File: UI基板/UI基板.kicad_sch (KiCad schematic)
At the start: 2 parts, among them U1 TFT_320x240

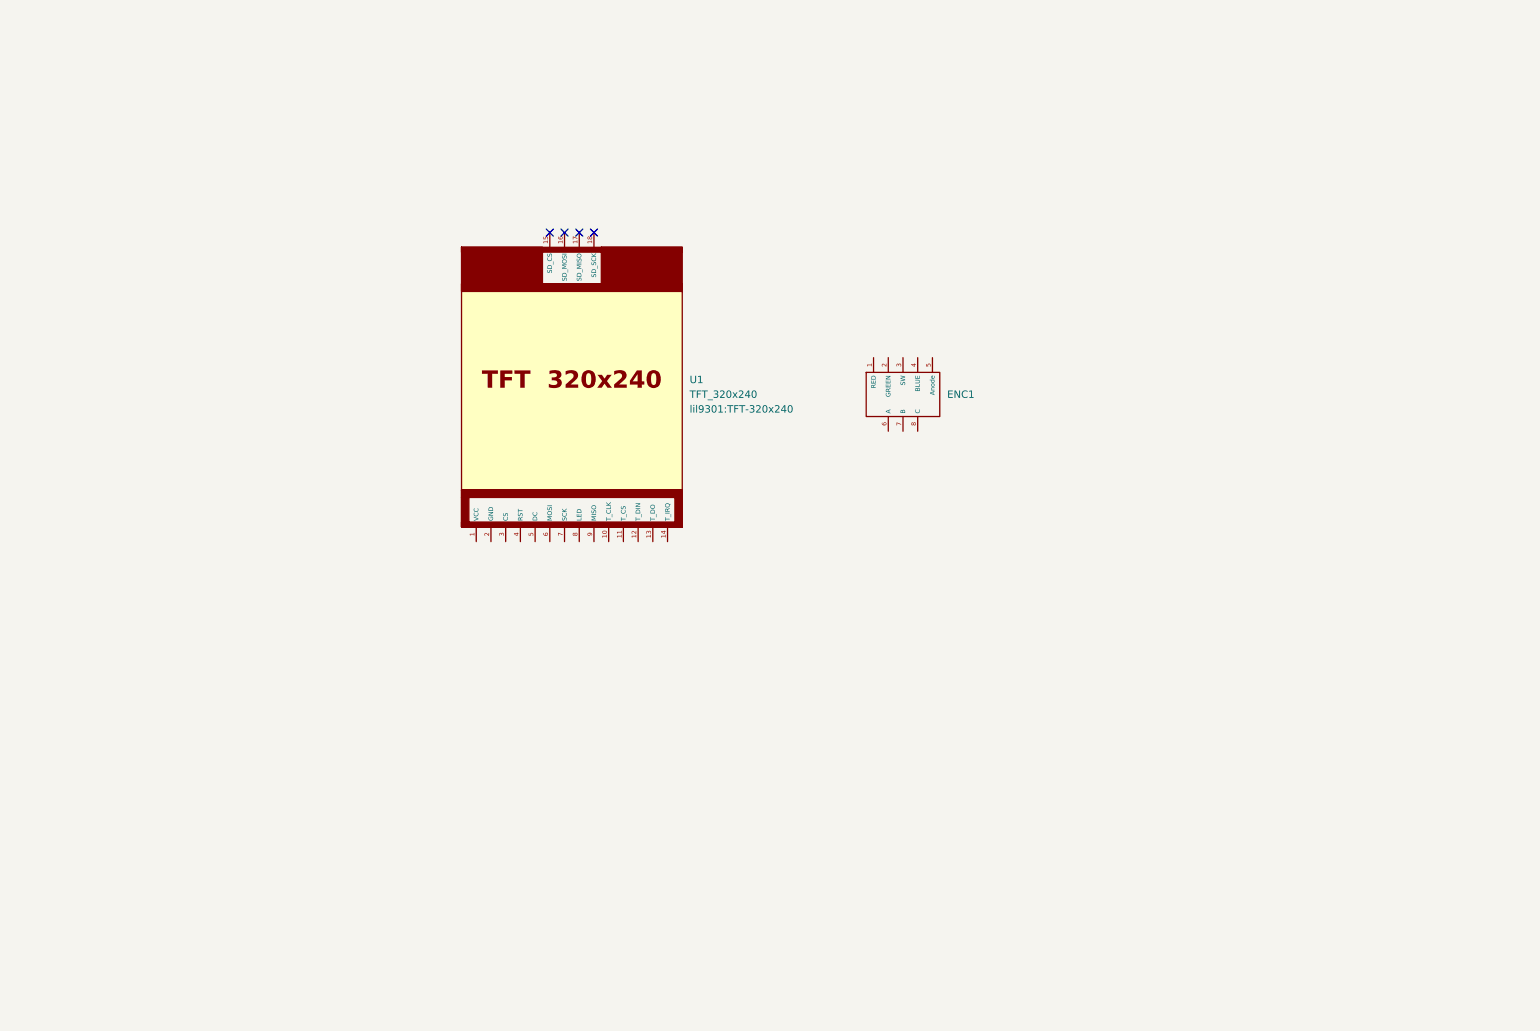
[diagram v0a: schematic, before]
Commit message: パスコンと保護ダイオードの追加
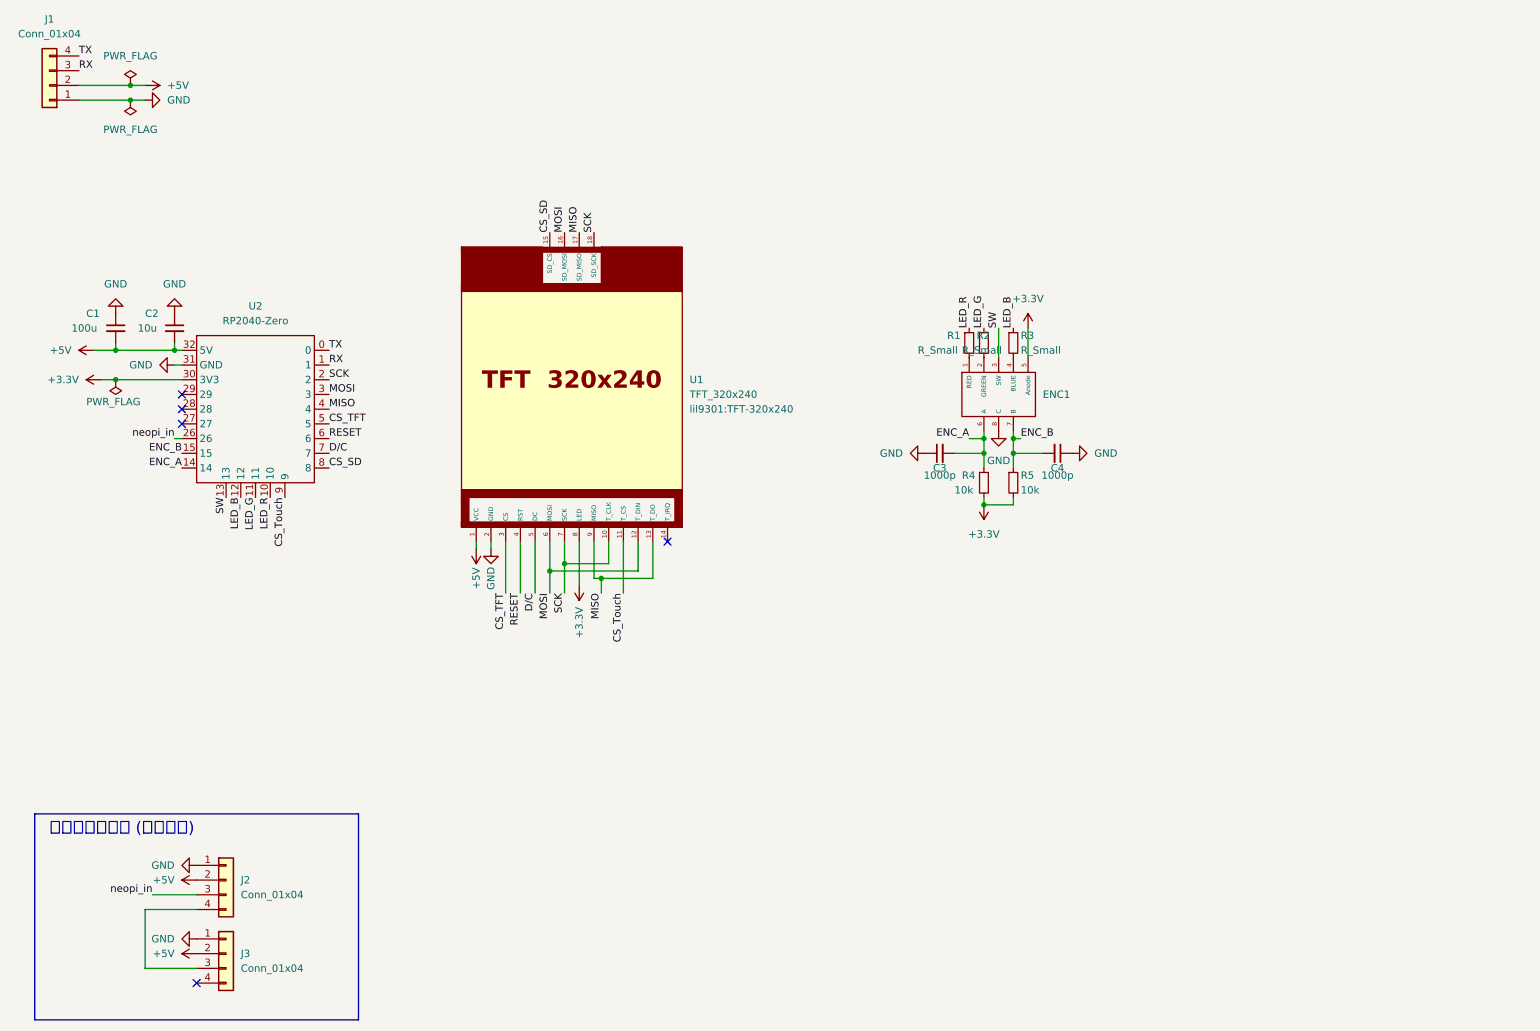
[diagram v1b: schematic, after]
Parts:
- added C1: 100u, Capacitor_THT:CP_Radial_D5.0mm_P2.50mm, symbol Device:C_Small
- added C2: 10u, Resistor_SMD:R_0603_1608Metric_Pad0.98x0.95mm_HandSolder, symbol Device:C_Small
- added C3, C4: 1000p, Capacitor_SMD:C_0603_1608Metric_Pad1.08x0.95mm_HandSolder, symbol Device:C_Small
- added J1, J2, J3: Conn_01x04, Connector_JST:JST_XH_S4B-XH-A_1x04_P2.50mm_Horizontal, symbol Connector_Generic:Conn_01x04
- added R1, R2, R3: R_Small, Resistor_SMD:R_0603_1608Metric_Pad0.98x0.95mm_HandSolder, symbol Device:R_Small
- added R4, R5: 10k, Resistor_SMD:R_0603_1608Metric_Pad0.98x0.95mm_HandSolder, symbol Device:R_Small
- added U2: RP2040-Zero, isw-kbd:RP2040-Zero-THT, symbol isw-mcu:RP2040-Zero
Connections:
- net +5V: now reaches U1.1 (VCC)
- net +5V: now also C1.2, C2.2, J1.2 (Pin_2), J2.2 (Pin_2), J3.2 (Pin_2), U2.32 (5V)
- net SCK: now reaches U1.10 (T_CLK)
- net SCK: now also U1.18 (SD_SCK), U1.7 (SCK), U2.2
- net CS_Touch: now reaches U1.11 (T_CS)
- net CS_Touch: now also U2.9
- net MOSI: now reaches U1.12 (T_DIN)
- net MOSI: now also U1.16 (SD_MOSI), U1.6 (MOSI), U2.3
- net MISO: now reaches U1.13 (T_DO)
- net MISO: now also U1.17 (SD_MISO), U1.9 (MISO), U2.4
- net CS_SD: now reaches U1.15 (SD_CS)
- net CS_SD: now also U2.8
- net GND: now reaches U1.2 (GND)
- net GND: now also ENC1.8 (C), C1.1, C2.1, C3.1, C4.1, J1.1 (Pin_1), J2.1 (Pin_1), J3.1 (Pin_1), U2.31 (GND)
- net CS_TFT: now reaches U1.3 (CS)
- net CS_TFT: now also U2.5
- net RESET: now reaches U1.4 (RST)
- net RESET: now also U2.6
- net D/C: now reaches U1.5 (DC)
- net D/C: now also U2.7
- net +3.3V: now reaches U1.8 (LED)
- net +3.3V: now also ENC1.5 (Anode), R4.2, R5.2, U2.30 (3V3)
- net at ENC1.1 (RED): now also R1.2
- net at ENC1.2 (GREEN): now also R2.2
- net SW: now reaches ENC1.3 (SW)
- net SW: now also U2.13
- net at ENC1.4 (BLUE): now also R3.2
- net ENC_A: now reaches ENC1.6 (A)
- net ENC_A: now also C3.2, R4.1, U2.14
- net ENC_B: now reaches ENC1.7 (B)
- net ENC_B: now also C4.2, R5.1, U2.15
- new net: J2.4 (Pin_4), J3.3 (Pin_3)
- new net LED_B: R3.1, U2.12
- new net LED_G: R2.1, U2.11
- new net LED_R: R1.1, U2.10
- new net RX: J1.3 (Pin_3), U2.1
- new net TX: J1.4 (Pin_4), U2.0
- new net neopi_in: J2.3 (Pin_3), U2.26
- no-connect marks 4 -> 5
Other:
- note added: "ネオピコネクタ (念のため)"
- moved on the sheet: ENC1

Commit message: ほげほげ
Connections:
- net RX renamed RX_in
- net RX_in: now also U2.0; no longer U2.1
- net TX renamed TX_in
- net TX_in: now also U2.1; no longer U2.0
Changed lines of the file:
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@@
 (kicad_sch (version 20230121) (generator eeschema)
   (paper "A4")
+  (junction (at 39.37 31.75) (diameter 0) (color 0 0 0 0)
+  )
   (junction (at 34.29 74.93) (diameter 0) (color 0 0 0 0)
   )
@@
   (junction (at 111.76 111.76) (diameter 0) (color 0 0 0 0)
   )
-  (junction (at 36.83 31.75) (diameter 0) (color 0 0 0 0)
-  )
   (junction (at 189.23 90.17) (diameter 0) (color 0 0 0 0)
   )
-  (junction (at 36.83 29.21) (diameter 0) (color 0 0 0 0)
-  )
   (junction (at 109.22 113.03) (diameter 0) (color 0 0 0 0)
+  )
+  (junction (at 39.37 29.21) (diameter 0) (color 0 0 0 0)
   )
   (junction (at 184.15 92.71) (diameter 0) (color 0 0 0 0)
@@
     (stroke (width 0) (type default))
   )
-  (wire (pts (xy 39.37 31.75) (xy 36.83 31.75))
+  (wire (pts (xy 41.91 31.75) (xy 39.37 31.75))
     (stroke (width 0) (type default))
   )
@@
     (stroke (width 0) (type default))
   )
-  (wire (pts (xy 36.83 31.75) (xy 27.94 31.75))
+  (wire (pts (xy 27.94 29.21) (xy 39.37 29.21))
+    (stroke (width 0) (type default))
+  )
+  (wire (pts (xy 27.94 31.75) (xy 39.37 31.75))
     (stroke (width 0) (type default))
   )
@@
     (stroke (width 0) (type default))
   )
-  (wire (pts (xy 36.83 29.21) (xy 27.94 29.21))
-    (stroke (width 0) (type default))
-  )
   (wire (pts (xy 194.31 92.71) (xy 189.23 92.71))
     (stroke (width 0) (type default))
@@
     (stroke (width 0) (type default))
   )
-  (wire (pts (xy 39.37 29.21) (xy 36.83 29.21))
+  (wire (pts (xy 41.91 29.21) (xy 39.37 29.21))
     (stroke (width 0) (type default))
   )
@@
     (effects (font (size 1.27 1.27)) (justify right bottom))
   )
-  (label "TX" (at 27.94 24.13 0) (fields_autoplaced)
+  (label "TX_in" (at 27.94 24.13 0) (fields_autoplaced)
     (effects (font (size 1.27 1.27)) (justify left bottom))
   )
@@
     (effects (font (size 1.27 1.27)) (justify left bottom))
   )
-  (label "TX" (at 71.12 74.93 0) (fields_autoplaced)
-    (effects (font (size 1.27 1.27)) (justify left bottom))
-  )
   (label "MOSI" (at 109.22 116.84 270) (fields_autoplaced)
     (effects (font (size 1.27 1.27)) (justify right bottom))
@@
     (effects (font (size 1.27 1.27)) (justify left bottom))
   )
-  (label "RX" (at 71.12 77.47 0) (fields_autoplaced)
-    (effects (font (size 1.27 1.27)) (justify left bottom))
-  )
   (label "LED_B" (at 55.88 100.33 270) (fields_autoplaced)
     (effects (font (size 1.27 1.27)) (justify right bottom))
@@
     (effects (font (size 1.27 1.27)) (justify left bottom))
   )
+  (label "RX_in" (at 71.12 74.93 0) (fields_autoplaced)
+    (effects (font (size 1.27 1.27)) (justify left bottom))
+  )
   (label "CS_Touch" (at 121.92 116.84 270) (fields_autoplaced)
     (effects (font (size 1.27 1.27)) (justify right bottom))
@@
     (effects (font (size 1.27 1.27)) (justify right bottom))
   )
+  (label "TX_in" (at 71.12 77.47 0) (fields_autoplaced)
+    (effects (font (size 1.27 1.27)) (justify left bottom))
+  )
   (label "SCK" (at 71.12 80.01 0) (fields_autoplaced)
     (effects (font (size 1.27 1.27)) (justify left bottom))
   )
-  (label "RX" (at 27.94 26.67 0) (fields_autoplaced)
+  (label "RX_in" (at 27.94 26.67 0) (fields_autoplaced)
     (effects (font (size 1.27 1.27)) (justify left bottom))
   )
@@
     )
   )
-  (symbol (lib_id "power:GND") (at 39.37 31.75 90) (unit 1)
-    (in_bom yes) (on_board yes) (dnp no) (fields_autoplaced)
-    (property "Reference" "#PWR02" (at 45.72 31.75 0)
-      (effects (font (size 1.27 1.27)) hide)
-    )
-    (property "Value" "GND" (at 43.18 31.75 90)
+  (symbol (lib_id "power:GND") (at 41.91 31.75 90) (unit 1)
+    (in_bom yes) (on_board yes) (dnp no) (fields_autoplaced)
+    (property "Reference" "#PWR02" (at 48.26 31.75 0)
+      (effects (font (size 1.27 1.27)) hide)
+    )
+    (property "Value" "GND" (at 45.72 31.75 90)
       (effects (font (size 1.27 1.27)) (justify right))
     )
-    (property "Footprint" "" (at 39.37 31.75 0)
-      (effects (font (size 1.27 1.27)) hide)
-    )
-    (property "Datasheet" "" (at 39.37 31.75 0)
+    (property "Footprint" "" (at 41.91 31.75 0)
+      (effects (font (size 1.27 1.27)) hide)
+    )
+    (property "Datasheet" "" (at 41.91 31.75 0)
       (effects (font (size 1.27 1.27)) hide)
     )
@@
     )
   )
-  (symbol (lib_id "power:PWR_FLAG") (at 36.83 31.75 180) (unit 1)
-    (in_bom yes) (on_board yes) (dnp no) (fields_autoplaced)
-    (property "Reference" "#FLG02" (at 36.83 33.655 0)
-      (effects (font (size 1.27 1.27)) hide)
-    )
-    (property "Value" "PWR_FLAG" (at 36.83 36.83 0)
-      (effects (font (size 1.27 1.27)))
-    )
-    (property "Footprint" "" (at 36.83 31.75 0)
-      (effects (font (size 1.27 1.27)) hide)
-    )
-    (property "Datasheet" "~" (at 36.83 31.75 0)
+  (symbol (lib_id "power:PWR_FLAG") (at 39.37 31.75 180) (unit 1)
+    (in_bom yes) (on_board yes) (dnp no) (fields_autoplaced)
+    (property "Reference" "#FLG02" (at 39.37 33.655 0)
+      (effects (font (size 1.27 1.27)) hide)
+    )
+    (property "Value" "PWR_FLAG" (at 39.37 36.83 0)
+      (effects (font (size 1.27 1.27)))
+    )
+    (property "Footprint" "" (at 39.37 31.75 0)
+      (effects (font (size 1.27 1.27)) hide)
+    )
+    (property "Datasheet" "~" (at 39.37 31.75 0)
       (effects (font (size 1.27 1.27)) hide)
     )
@@
     )
   )
-  (symbol (lib_id "power:+5V") (at 39.37 29.21 270) (unit 1)
-    (in_bom yes) (on_board yes) (dnp no) (fields_autoplaced)
-    (property "Reference" "#PWR01" (at 35.56 29.21 0)
-      (effects (font (size 1.27 1.27)) hide)
-    )
-    (property "Value" "+5V" (at 43.18 29.21 90)
-      (effects (font (size 1.27 1.27)) (justify left))
-    )
-    (property "Footprint" "" (at 39.37 29.21 0)
-      (effects (font (size 1.27 1.27)) hide)
-    )
-    (property "Datasheet" "" (at 39.37 29.21 0)
+  (symbol (lib_id "power:+5V") (at 41.91 29.21 270) (unit 1)
+    (in_bom yes) (on_board yes) (dnp no) (fields_autoplaced)
+    (property "Reference" "#PWR01" (at 38.1 29.21 0)
+      (effects (font (size 1.27 1.27)) hide)
+    )
+    (property "Value" "+5V" (at 45.72 29.21 90)
+      (effects (font (size 1.27 1.27)) (justify left))
+    )
+    (property "Footprint" "" (at 41.91 29.21 0)
+      (effects (font (size 1.27 1.27)) hide)
+    )
+    (property "Datasheet" "" (at 41.91 29.21 0)
       (effects (font (size 1.27 1.27)) hide)
     )
@@
     )
   )
-  (symbol (lib_id "power:PWR_FLAG") (at 36.83 29.21 0) (unit 1)
-    (in_bom yes) (on_board yes) (dnp no) (fields_autoplaced)
-    (property "Reference" "#FLG01" (at 36.83 27.305 0)
-      (effects (font (size 1.27 1.27)) hide)
-    )
-    (property "Value" "PWR_FLAG" (at 36.83 24.13 0)
-      (effects (font (size 1.27 1.27)))
-    )
-    (property "Footprint" "" (at 36.83 29.21 0)
-      (effects (font (size 1.27 1.27)) hide)
-    )
-    (property "Datasheet" "~" (at 36.83 29.21 0)
-      (effects (font (size 1.27 1.27)) hide)
-    )
+  (symbol (lib_id "power:PWR_FLAG") (at 39.37 29.21 0) (unit 1)
+    (in_bom yes) (on_board yes) (dnp no) (fields_autoplaced)
+    (property "Reference" "#FLG01" (at 39.37 27.305 0)
+      (effects (font (size 1.27 1.27)) hide)
+    )
+    (property "Value" "PWR_FLAG" (at 39.37 24.13 0)
+      (effects (font (size 1.27 1.27)))
+    )
+    (property "Footprint" "" (at 39.37 29.21 0)
+      (effects (font (size 1.27 1.27)) hide)
+    )
+    (property "Datasheet" "~" (at 39.37 29.21 0)
+      (effects (font (size 1.27 1.27)) hide)
+    )

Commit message: サーボ基板
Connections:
- net RX_in renamed RX_main
- net TX_in renamed TX_main

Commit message: メイン基板
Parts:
- removed C1: 100u, Capacitor_THT:CP_Radial_D5.0mm_P2.50mm, symbol Device:C_Small
- removed C2: 10u, Resistor_SMD:R_0603_1608Metric_Pad0.98x0.95mm_HandSolder, symbol Device:C_Small
- removed J2, J3: Conn_01x04, Connector_JST:JST_XH_S4B-XH-A_1x04_P2.50mm_Horizontal, symbol Connector_Generic:Conn_01x04
- removed U2: RP2040-Zero, isw-kbd:RP2040-Zero-THT, symbol isw-mcu:RP2040-Zero
- added C1: C_Polarized_Small, Capacitor_THT:CP_Radial_D5.0mm_P2.50mm, symbol Device:C_Polarized_Small
- added J2, J4: Conn_01x03, Connector_JST:JST_XH_S3B-XH-A_1x03_P2.50mm_Horizontal, symbol Connector_Generic:Conn_01x03
- added J5: Conn_01x04, OPL_Connector:GROVE-HW4-2.0-90D, symbol Connector_Generic:Conn_01x04
- added SW1: SW_Push, Button_Switch_THT:SW_PUSH_6mm_H4.3mm, symbol Switch:SW_Push
- added SW2: ~, ハンドル基板:TTP223, symbol TTP223:TTP223
- added U3: Pico, MCU_RaspberryPi_and_Boards:RPi_Pico_SMD_TH, symbol MCU_RaspberryPi_and_Boards:Pico
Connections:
- net +3.3V: now also U3.36 (3V3)
- net +5V: now also J1.1 (Pin_1), C1.2, J4.1 (Pin_1), J5.3 (Pin_3), U3.39 (VSYS); no longer J1.2 (Pin_2)
- net CS_SD: now also U3.27 (GPIO21)
- net CS_TFT: now also U3.22 (GPIO17)
- net CS_Touch: now also U3.26 (GPIO20)
- net D/C: now also U3.29 (GPIO22)
- net ENC_A: now also U3.17 (GPIO13)
- net ENC_B: now also U3.16 (GPIO12)
- net GND: now also J1.2 (Pin_2), C1.1, J2.3 (Pin_3), J4.3 (Pin_3), J5.4 (Pin_4), SW1.2, SW2.3 (GND), U3.13 (GND), U3.18 (GND), U3.23 (GND), U3.28 (GND), U3.3 (GND), U3.38 (GND), U3.8 (GND); no longer J1.1 (Pin_1)
- net LED_B: now also U3.10 (GPIO7)
- net LED_G: now also U3.11 (GPIO8)
- net LED_R: now also U3.12 (GPIO9)
- net MISO: now also U3.21 (GPIO16)
- net MOSI: now also U3.25 (GPIO19)
- net RESET: now also U3.31 (GPIO26_ADC0)
- net RX_main: now also U3.1 (GPIO0)
- net SCK: now also U3.24 (GPIO18)
- net SW: now also U3.15 (GPIO11)
- net TX_main: now also U3.2 (GPIO1)
- net neopi_in: now also J5.2 (Pin_2), U3.20 (GPIO15)
- new net: J2.1 (Pin_1), SW2.1 (Vcc)
- new net: J2.2 (Pin_2), SW2.2 (IO)
- new net IO: J4.2 (Pin_2), U3.32 (GPIO27_ADC1)
- new net enable_pico: SW1.1, U3.30 (RUN)
- no-connect marks 5 -> 17
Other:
- note removed: "ネオピコネクタ (念のため)"
